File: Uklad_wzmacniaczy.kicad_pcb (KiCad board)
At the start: 4 copper layers, 80 x 120 mm, 107 parts, among them J1 SJ1-3523N, J2 MEM2080-00-128-00-A, J3 Conn_01x10_Pin, U1 OPA2388IDR, U10 AD5162BRMZ10-RL7, U11 AD5162BRMZ10-RL7, U12 LT3094EMSE-TRPBF, U13 Nucleo-H755ZIQ-Morpho, U14 TPS61236PRWLR, U15 LD1117S50TR_SOT223, U2 REF2033QDDCRQ1, U3 AD8421ARMZ, U4 OPA388IDR, U5 AD8421ARMZ, U6 TPD4E1B06DRLR, U7 AD5162BRMZ10-RL7, U8 LT3042EMSE-TRPBF, U9 TPS65135RTER

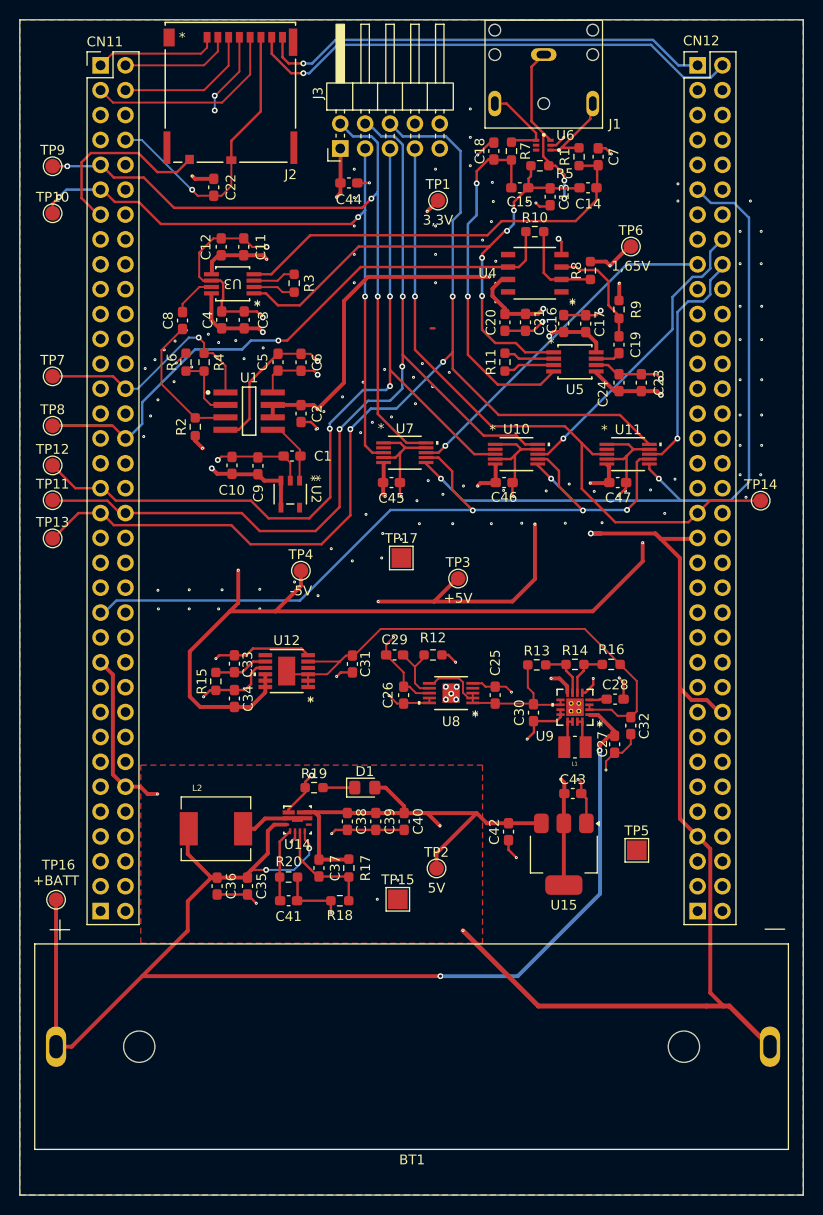
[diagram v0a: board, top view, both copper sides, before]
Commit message: Errors in pcb layout removed, footprints fixed, microvias changed to regular vias
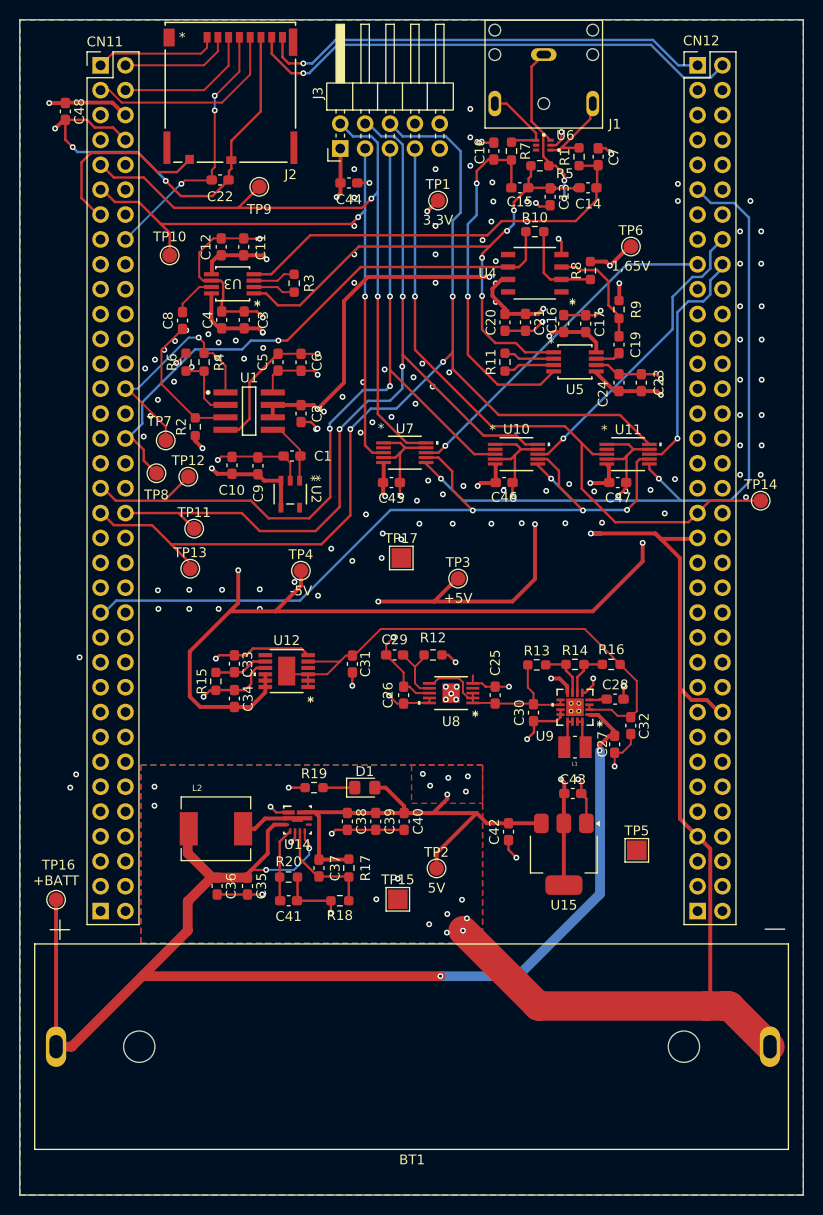
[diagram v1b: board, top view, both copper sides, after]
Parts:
- added C48: 10u, Capacitor_SMD:C_0603_1608Metric_Pad1.08x0.95mm_HandSolder, F.Cu at (110.2, 32.2)
- moved TP9 21.2 mm to (130.1, 39.9)
- moved TP11 14.7 mm to (123.4, 74.8)
- moved TP13 14.4 mm to (123.0, 78.9)
- moved TP12 13.9 mm to (122.8, 69.5)
- moved TP7 13.3 mm to (120.5, 65.8)
- moved TP10 12.7 mm to (120.9, 46.9)
- moved TP8 11.7 mm to (119.5, 69.2)
- moved C22 0.99 mm to (126.0, 39.2), turned to 0 degrees
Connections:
- C22 pad 1: +3.3V -> +3.3V_Nucleo
- J2 pad P4: +3.3V -> +3.3V_Nucleo
- U13 pad 1.06: unconnected-(U13-5V_EXT-Pad1.06) -> +5V
- U13 pad 1.16: unconnected-(U13-3V3-Pad1.16) -> +3.3V_Nucleo
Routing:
- net +3.3V_Nucleo: track 0.00 -> 27.1 mm, vias 0 -> 3
- net +5V: track 46.8 -> 65.1 mm, vias 1 -> 9
- net +3.3V: track 58.6 -> 47.8 mm, vias 12 -> 9
- net GND: track 175.5 -> 184.5 mm, vias 10 -> 20
- net /TO_ADC2: track 66.4 -> 57.9 mm
- net /SIG_3: track 94.9 -> 89.2 mm
- net GNDA: track 166.1 -> 162.8 mm
- net /SIG_2: track 68.0 -> 65.1 mm, vias 3 -> 2
- net /SIG_5: track 110.7 -> 108.1 mm
- net /SIG_4: track 85.4 -> 83.0 mm
- net /SIG_1: track 74.2 -> 72.5 mm, vias 3 -> 2
- net /TO_ADC1: track 24.7 -> 24.0 mm
- added copper zone on F.Cu, net +5V
- added copper zone on B.Cu, net GND

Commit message: Vias fixed, generated gerber files
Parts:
- R10, R4: value 200-400k -> 220k
- U15: value LD1117S50TR_SOT223 -> LD1117S33TR_SOT223
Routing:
- net /Reference_In: track 18.0 -> 13.6 mm, vias 2 -> 0
- net +1.65VA: track 88.4 -> 89.6 mm
- net GNDA: track 162.8 -> 163.3 mm, vias 143 -> 81
